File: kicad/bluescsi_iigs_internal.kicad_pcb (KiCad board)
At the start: 2 copper layers, 61.5 x 55.4 mm, 27 parts, among them J1 Conn_02x13_Odd_Even, J2 Conn_02x13_Odd_Even, J3 105162-0001, J4 Conn_01x02_Male, J5 Conn_01x02_Male, J6 DB25_Male, M1 Screw_Terminal_01x01, M2 Screw_Terminal_01x01, SW1 SW_SPDT, U1 YAAJ_BluePill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

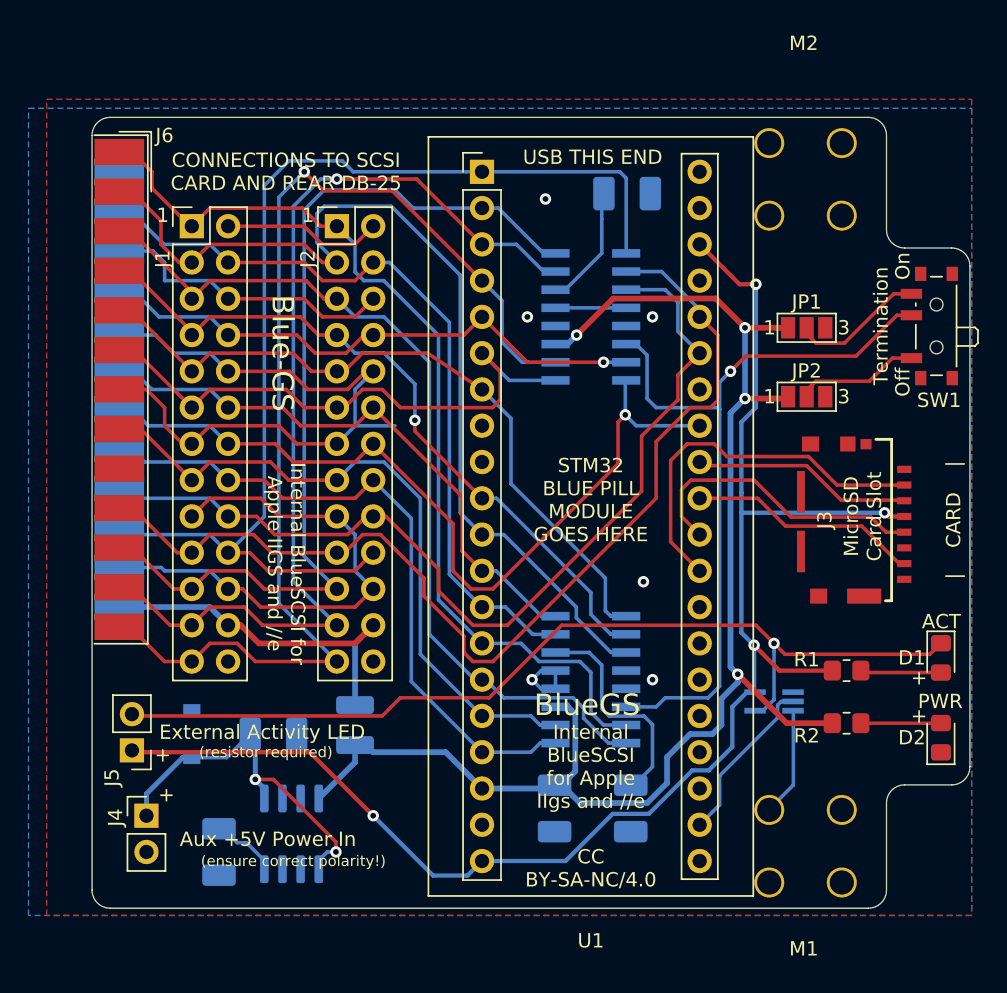
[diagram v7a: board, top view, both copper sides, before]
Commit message: Move power and led headers to better positon; Add indentation around microsd slot
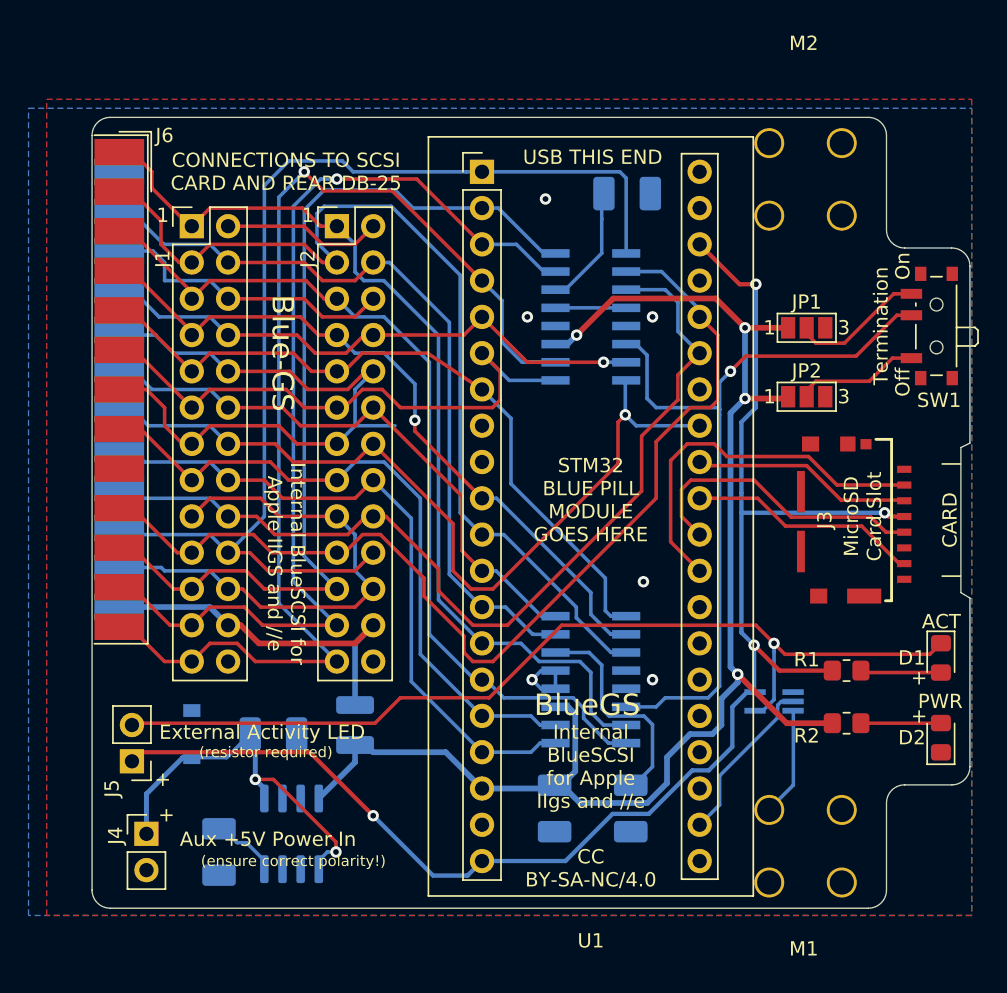
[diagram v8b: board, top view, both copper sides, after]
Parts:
- moved J4 1.27 mm to (128.9, 97.2)
- moved J5 0.76 mm to (127.9, 92.1)
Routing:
- net /+5V_AUX: track 25.7 -> 26.9 mm
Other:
- outline, holes or cut-outs redrawn
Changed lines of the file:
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@@
   )
   (footprint "Connector_PinHeader_2.54mm:PinHeader_1x02_P2.54mm_Vertical" (layer "F.Cu")
-    (at 128.905 95.885)
+    (at 128.905 97.155)
     (descr "Through hole straight pin header, 1x02, 2.54mm pitch, single row")
     (tags "Through hole pin header THT 1x02 2.54mm single row")
@@
   )
   (footprint "Connector_PinHeader_2.54mm:PinHeader_1x02_P2.54mm_Vertical" (layer "F.Cu")
-    (at 127.889 91.313 180)
+    (at 127.889 92.075 180)
     (descr "Through hole straight pin header, 1x02, 2.54mm pitch, single row")
     (tags "Through hole pin header THT 1x02 2.54mm single row")
@@
     )
   )
-  (gr_line (start 186.563 57.404) (end 186.563 92.456) (layer "Edge.Cuts") (width 0.05))
+  (gr_line (start 186.563 80.645) (end 186.563 92.456) (layer "Edge.Cuts") (width 0.05))
   (gr_line (start 125.095 101.092) (end 125.095 48.26) (layer "Edge.Cuts") (width 0.05))
   (gr_line (start 181.991 56.134) (end 185.293 56.134) (layer "Edge.Cuts") (width 0.05))
@@
   (gr_line (start 179.451 102.362) (end 126.365 102.362) (layer "Edge.Cuts") (width 0.05))
   (gr_arc (start 126.365 102.362) (mid 125.466974 101.990026) (end 125.095 101.092) (layer "Edge.Cuts") (width 0.05))
+  (gr_line (start 185.928 70.104) (end 185.928 80.264) (layer "Edge.Cuts") (width 0.05))
   (gr_arc (start 180.721 101.092) (mid 180.349026 101.990026) (end 179.451 102.362) (layer "Edge.Cuts") (width 0.05))
   (gr_arc (start 125.095 48.26) (mid 125.466974 47.361974) (end 126.365 46.99) (layer "Edge.Cuts") (width 0.05))
+  (gr_line (start 186.563 57.404) (end 186.563 69.7992) (layer "Edge.Cuts") (width 0.05))
+  (gr_line (start 185.928 70.104) (end 186.563 69.7992) (layer "Edge.Cuts") (width 0.05))
   (gr_arc (start 179.451 46.99) (mid 180.349026 47.361974) (end 180.721 48.26) (layer "Edge.Cuts") (width 0.05))
+  (gr_line (start 186.563 80.645) (end 185.928 80.264) (layer "Edge.Cuts") (width 0.05))
   (gr_text "ACT" (at 185.42 85.09 90) (layer "B.SilkS")
     (effects (font (size 1 1) (thickness 0.15)) (justify mirror))
@@
     (effects (font (size 1 1) (thickness 0.15)) (justify mirror))
   )
-  (gr_text "|    CARD    |" (at 185.42 75.184 90) (layer "B.SilkS")
+  (gr_text "|    CARD    |" (at 185.166 75.184 90) (layer "B.SilkS")
     (effects (font (size 1 1) (thickness 0.15)) (justify mirror))
   )
@@
     (effects (font (size 1.5 1.5) (thickness 0.15)))
   )
-  (gr_text "+" (at 130.048 91.694 180) (layer "F.SilkS")
+  (gr_text "+" (at 130.048 93.405 180) (layer "F.SilkS")
     (effects (font (size 1 1) (thickness 0.15)))
   )
@@
     (effects (font (size 1 1) (thickness 0.15)))
   )
-  (gr_text "|    CARD    |" (at 185.42 75.184 90) (layer "F.SilkS")
+  (gr_text "|    CARD    |" (at 185.166 75.184 90) (layer "F.SilkS")
     (effects (font (size 1 1) (thickness 0.15)))
   )
@@
     (effects (font (size 0.75 0.75) (thickness 0.125)) (justify left))
   )
-  (gr_text "+" (at 130.302 94.488 180) (layer "F.SilkS")
+  (gr_text "+" (at 130.302 95.885 180) (layer "F.SilkS")
     (effects (font (size 1 1) (thickness 0.15)))
   )
@@
   (segment (start 171.45 72.39) (end 174.037511 74.977511) (width 0.25) (layer "F.Cu") (net 33))
   (segment (start 180.682 76.034) (end 181.965 76.034) (width 0.25) (layer "F.Cu") (net 33))
+  (segment (start 140.335 91.44) (end 128.524 91.44) (width 0.3) (layer "F.Cu") (net 34))
   (segment (start 180.594 74.676) (end 180.852 74.934) (width 0.3) (layer "F.Cu") (net 34))
   (segment (start 173.228 85.725) (end 171.45 83.947) (width 0.3) (layer "F.Cu") (net 34))
+  (segment (start 128.524 91.44) (end 127.889 92.075) (width 0.3) (layer "F.Cu") (net 34))
+  (segment (start 144.78 95.885) (end 140.335 91.44) (width 0.3) (layer "F.Cu") (net 34))
   (segment (start 180.852 74.934) (end 181.965 74.934) (width 0.3) (layer "F.Cu") (net 34))
-  (segment (start 128.016 91.44) (end 127.889 91.313) (width 0.3) (layer "F.Cu") (net 34))
-  (segment (start 140.335 91.44) (end 128.016 91.44) (width 0.3) (layer "F.Cu") (net 34))
   (segment (start 167.64 55.88) (end 170.434 58.674) (width 0.3) (layer "F.Cu") (net 34))
   (segment (start 170.434 58.674) (end 171.577 58.674) (width 0.3) (layer "F.Cu") (net 34))
   (segment (start 176.927 85.725) (end 173.228 85.725) (width 0.3) (layer "F.Cu") (net 34))
-  (segment (start 144.78 95.885) (end 140.335 91.44) (width 0.3) (layer "F.Cu") (net 34))
   (via (at 171.45 83.947) (size 0.8) (drill 0.4) (layers "F.Cu" "B.Cu") (net 34))
   (via (at 180.594 74.676) (size 0.8) (drill 0.4) (layers "F.Cu" "B.Cu") (net 34))
@@
   (segment (start 163.957 63.642) (end 163.957 66.675) (width 0.25) (layer "B.Cu") (net 42))
   (segment (start 165.227 87.63) (end 164.592 88.265) (width 0.25) (layer "B.Cu") (net 42))
+  (segment (start 172.847 83.82) (end 171.577 82.55) (width 0.25) (layer "F.Cu") (net 43))
   (segment (start 157.978251 82.55) (end 152.898251 87.63) (width 0.25) (layer "F.Cu") (net 43))
+  (segment (start 128.016 89.408) (end 127.889 89.535) (width 0.25) (layer "F.Cu") (net 43))
+  (segment (start 171.577 82.55) (end 157.978251 82.55) (width 0.25) (layer "F.Cu") (net 43))
   (segment (start 152.898251 87.63) (end 146.685 87.63) (width 0.25) (layer "F.Cu") (net 43))
-  (segment (start 172.847 83.82) (end 171.577 82.55) (width 0.25) (layer "F.Cu") (net 43))
-  (segment (start 128.016 88.9) (end 127.889 88.773) (width 0.25) (layer "F.Cu") (net 43))
-  (segment (start 146.685 87.63) (end 145.415 88.9) (width 0.25) (layer "F.Cu") (net 43))
-  (segment (start 171.577 82.55) (end 157.978251 82.55) (width 0.25) (layer "F.Cu") (net 43))
+  (segment (start 144.907 89.408) (end 128.016 89.408) (width 0.25) (layer "F.Cu") (net 43))
+  (segment (start 146.685 87.63) (end 144.907 89.408) (width 0.25) (layer "F.Cu") (net 43))
   (segment (start 183.76 84.582) (end 173.609 84.582) (width 0.25) (layer "F.Cu") (net 43))
-  (segment (start 145.415 88.9) (end 128.016 88.9) (width 0.25) (layer "F.Cu") (net 43))
   (segment (start 173.609 84.582) (end 172.847 83.82) (width 0.25) (layer "F.Cu") (net 43))
   (segment (start 184.531 83.811) (end 183.76 84.582) (width 0.25) (layer "F.Cu") (net 43))
@@
   (via (at 136.525 93.345) (size 0.8) (drill 0.4) (layers "F.Cu" "B.Cu") (net 46))
   (via (at 142.175 98.425) (size 0.8) (drill 0.4) (layers "F.Cu" "B.Cu") (net 46))
+  (segment (start 128.905 94.36) (end 131.445 91.82) (width 0.35) (layer "B.Cu") (net 46))
   (segment (start 142.175 98.425) (end 141.5725 98.425) (width 0.25) (layer "B.Cu") (net 46))
   (segment (start 134.52 91.82) (end 136.17 90.17) (width 0.25) (layer "B.Cu") (net 46))
-  (segment (start 128.905 94.36) (end 131.445 91.82) (width 0.35) (layer "B.Cu") (net 46))
   (segment (start 141.5725 98.425) (end 140.97 99.0275) (width 0.25) (layer "B.Cu") (net 46))
-  (segment (start 128.905 95.885) (end 128.905 94.36) (width 0.35) (layer "B.Cu") (net 46))
   (segment (start 137.16 93.98) (end 136.525 93.345) (width 0.35) (layer "B.Cu") (net 46))
+  (segment (start 128.905 97.155) (end 128.905 94.36) (width 0.35) (layer "B.Cu") (net 46))
+  (segment (start 131.445 91.82) (end 132.08 91.82) (width 0.35) (layer "B.Cu") (net 46))
   (segment (start 136.525 90.525) (end 136.17 90.17) (width 0.35) (layer "B.Cu") (net 46))
   (segment (start 132.08 91.82) (end 134.52 91.82) (width 0.25) (layer "B.Cu") (net 46))
   (segment (start 137.16 94.68) (end 137.16 93.98) (width 0.35) (layer "B.Cu") (net 46))
   (segment (start 140.97 99.0275) (end 140.97 99.63) (width 0.25) (layer "B.Cu") (net 46))
-  (segment (start 131.445 91.82) (end 132.08 91.82) (width 0.35) (layer "B.Cu") (net 46))
   (segment (start 136.525 93.345) (end 136.525 90.525) (width 0.35) (layer "B.Cu") (net 46))
   (segment (start 135.255 97.77375) (end 135.90625 97.77375) (width 0.25) (layer "B.Cu") (net 47))
